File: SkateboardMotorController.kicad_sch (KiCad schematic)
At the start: 0 parts

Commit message: Added STM32
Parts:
- added C1: 0.1uF, symbol Device:C
- added FB1: FerriteBead, symbol Device:FerriteBead
- added U1: STM32F103C4Tx, Package_QFP:LQFP-48_7x7mm_P0.5mm, symbol MCU_ST_STM32F1:STM32F103C4Tx
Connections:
- new net: FB1.1, U1.9 (VDDA)
- new net +3.3V: C1.1, C1.2, FB1.2, U1.23 (VSS), U1.24 (VDD), U1.35 (VSS), U1.36 (VDD), U1.47 (VSS), U1.48 (VDD)

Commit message: finished most of STM32 and started on Gate drivers
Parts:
- added C2, C3, C4, C5: 0.1uF, symbol Device:C
- added R1, R2, R3: 10k, symbol Device:R
- added R4, R5: 10K, symbol Device:R
- added U2, U3, U5: IRS2104, Package_SO:SOIC-8_3.9x4.9mm_P1.27mm, symbol Driver_FET:IRS2104
- added Y1: MAX7375AXR805, Package_TO_SOT_SMD:SOT-323_SC-70, symbol Oscillator:MAX7375AXR805
- C1, FB1, U1: Manufacturer (none) -> Digikey
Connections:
- net +3.3V: now also C4.2, R1.1, R5.1, Y1.1 (V+); no longer C1.2, U1.23 (VSS), U1.35 (VSS), U1.47 (VSS)
- net Emergency Shutoff: now reaches U1.10 (PA0)
- net Emergency Shutoff: now also R5.2, U5.3 (~{SD})
- net at U1.20 (PB2): now also R3.1
- net PhaseA: now reaches U1.29 (PA8)
- net PhaseA: now also R4.1, U5.2 (IN)
- net at U1.44 (BOOT0): now also R2.1
- net at U1.5 (PD0): now also Y1.2 (CLOCK)
- net at U1.7 (NRST): now also C3.1, R1.2
- net GND: now reaches U1.8 (VSSA)
- net GND: now also C1.2, U1.23 (VSS), U1.35 (VSS), U1.47 (VSS), C2.2, C3.2, C4.1, C5.1, R2.2, R3.2, R4.2, U5.4 (COM), Y1.3 (GND)
- net at FB1.1, U1.9 (VDDA): now also C2.1
- new net +12V: C5.2, U5.1 (VCC)
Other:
- note added: "Gate Drivers"
- note added: "STM32 Microcontroller"
- moved on the sheet: FB1

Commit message: progress on gate drivers and found 60V-12V converter
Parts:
- added MP1: MP9486, Package_SO:SOIC-8-1EP_3.9x4.9mm_P1.27mm_EP2.41x3.3mm_ThermalVias, symbol MyLibrary:MP9486
- added R6, R7: 22, symbol Device:R
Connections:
- net at U5.5 (LO): now also R6.1
- net at U5.7 (HO): now also R7.1
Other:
- moved on the sheet: U2
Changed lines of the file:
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@@
+	)
+	(symbol
+		(lib_id "MyLibrary:MP9486")
+		(at 83.82 177.8 0)
+		(unit 1)
+		(exclude_from_sim no)
+		(in_bom yes)
+		(on_board yes)
+		(dnp no)
+		(property "Reference" "MP1"
+			(at 84.074 188.214 0)
+			(effects
+				(font
+					(size 1.27 1.27)
+				)
+			)
+		)
+		(property "Value" "MP9486"
+			(at 83.82 168.91 0)
+			(effects
+				(font
+					(size 1.27 1.27)
+				)
+			)
+		)
+		(property "Footprint" "Package_SO:SOIC-8-1EP_3.9x4.9mm_P1.27mm_EP2.41x3.3mm_ThermalVias"
+			(at 83.312 168.91 0)
+			(effects
+				(font
+					(size 1.27 1.27)
+				)
+				(hide yes)
+			)
+		)
+		(property "Datasheet" "https://www.monolithicpower.com/en/documentview/productdocument/index/version/2/document_type/Datasheet/lang/en/sku/MP9486/?srsltid=AU7gw4WBPXX73u71-zxU3O6eeoUXKs0Tn8aKEEhdp0QPcMegq4pCLmCL"
+			(at 83.82 177.8 0)
+			(effects
+				(font
+					(size 1.27 1.27)
+				)
+				(hide yes)
+			)
+		)
+		(property "Description" "60V -> 12V Buck converter, 1A max"
+			(at 83.82 177.8 0)
+			(effects
+				(font
+					(size 1.27 1.27)
+				)
+				(hide yes)
+			)
+		)
+		(property "Manufactuer PN" "MP9486GN-Z"
+			(at 83.82 177.8 0)
+			(effects
+				(font
+					(size 1.27 1.27)
+				)
+				(hide yes)
+			)
+		)
+		(property "Manufacturer" "JLCpcb"
+			(at 83.82 177.8 0)
+			(effects
+				(font
+					(size 1.27 1.27)
+				)
+				(hide yes)
+			)
+		)
+		(pin "4"
+		)
+		(pin "1"
+		)
+		(pin "6"
+		)
+		(pin "8"
+		)
+		(pin "7"
+		)
+		(pin "3"
+		)
+		(pin "2"
+		)
+		(pin "5"
+		)
+		(instances
+			(project ""
+				(path "/51090867-fcd4-4552-acda-4929fd1c7810"
+					(reference "MP1")
+					(unit 1)
+				)
+			)
+		)
 	)
 	(symbol
@@
 	(symbol
 		(lib_id "Driver_FET:IRS2104")
-		(at 271.78 58.42 0)
+		(at 283.21 57.15 0)
 		(unit 1)
 		(exclude_from_sim no)
@@
 		(fields_autoplaced yes)
 		(property "Reference" "U2"
-			(at 273.9233 43.18 0)
+			(at 285.3533 41.91 0)
 			(effects
 				(font
@@
 		)
 		(property "Value" "IRS2104"
-			(at 273.9233 45.72 0)
+			(at 285.3533 44.45 0)
 			(effects
 				(font
@@
 		)
 		(property "Footprint" "Package_SO:SOIC-8_3.9x4.9mm_P1.27mm"
-			(at 271.78 58.42 0)
+			(at 283.21 57.15 0)
 			(effects
 				(font
@@
 		)
 		(property "Datasheet" "https://www.infineon.com/dgdl/irs2104.pdf?fileId=5546d462533600a40153567633f727a1"
-			(at 271.78 58.42 0)
+			(at 283.21 57.15 0)
 			(effects
 				(font
@@
 		)
 		(property "Description" "Half-Bridge Driver, 600V, 290/600mA, PDIP-8/SOIC-8"
-			(at 271.78 58.42 0)
+			(at 283.21 57.15 0)
 			(effects
 				(font
@@
 	(symbol
 		(lib_id "Device:R")
+		(at 251.46 53.34 90)
+		(unit 1)
+		(exclude_from_sim no)
+		(in_bom yes)
+		(on_board yes)
+		(dnp no)
+		(fields_autoplaced yes)
+		(property "Reference" "R7"
+			(at 251.46 46.99 90)
+			(effects
+				(font
+					(size 1.27 1.27)
+				)
+			)
+		)
+		(property "Value" "22"
+			(at 251.46 49.53 90)
+			(effects
+				(font
+					(size 1.27 1.27)
+				)
+			)
+		)
+		(property "Footprint" ""
+			(at 251.46 55.118 90)
+			(effects
+				(font
+					(size 1.27 1.27)
+				)
+				(hide yes)
+			)
+		)
+		(property "Datasheet" "~"
+			(at 251.46 53.34 0)
+			(effects
+				(font
+					(size 1.27 1.27)
+				)
+				(hide yes)
+			)
+		)
+		(property "Description" "Resistor"
+			(at 251.46 53.34 0)
+			(effects
+				(font
+					(size 1.27 1.27)
+				)
+				(hide yes)
+			)
+		)
+		(pin "2"
+		)
+		(pin "1"
+		)
+		(instances
+			(project "SkateboardMotorController"
+				(path "/51090867-fcd4-4552-acda-4929fd1c7810"
+					(reference "R7")
+					(unit 1)
+				)
+			)
+		)
+	)
+	(symbol
+		(lib_id "Device:R")
 		(at 120.65 90.17 0)
 		(unit 1)
@@
 					(unit 1)
 				)
+			)
+		)
+	)
+	(symbol
+		(lib_id "Device:R")
+		(at 251.46 66.04 90)
+		(unit 1)
+		(exclude_from_sim no)
+		(in_bom yes)
+		(on_board yes)
+		(dnp no)
+		(fields_autoplaced yes)
+		(property "Reference" "R6"
+			(at 251.46 59.69 90)
+			(effects
+				(font
+					(size 1.27 1.27)
+				)
+			)
+		)
+		(property "Value" "22"
+			(at 251.46 62.23 90)
+			(effects
+				(font
+					(size 1.27 1.27)
+				)
+			)
+		)
+		(property "Footprint" ""
+			(at 251.46 67.818 90)
+			(effects
+				(font
+					(size 1.27 1.27)
+				)
+				(hide yes)
+			)
+		)
+		(property "Datasheet" "~"
+			(at 251.46 66.04 0)
+			(effects
+				(font
+					(size 1.27 1.27)
+				)
+				(hide yes)
+			)
+		)
+		(property "Description" "Resistor"
+			(at 251.46 66.04 0)
+			(effects
+				(font
+					(size 1.27 1.27)
+				)
+				(hide yes)
+			)
+		)
+		(pin "2"
+		)
+		(pin "1"
+		)
+		(instances
+			(project ""
+				(path "/51090867-fcd4-4552-acda-4929fd1c7810"
+					(reference "R6")
+					(unit 1)
+				)

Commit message: finished 12V rail
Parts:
- added B1100LB-13-F: 1A/100V, Diode_SMD:D_SMB, symbol Device:D_Schottky
- added C10: 10uF, Capacitor_SMD:C_0805_2012Metric, symbol Device:C
- added C11: 100uF/25V, Capacitor_Tantalum_SMD:CP_EIA-7343-43_Kemet-X, symbol Device:C_Polarized
- added C6, C8: 2.2uF/100V, Capacitor_SMD:C_1206_3216Metric, symbol Device:C
- added C7, C9: 0.1uF, Capacitor_SMD:C_0603_1608Metric, symbol Device:C
- added L1: 47uH, Inductor_SMD:L_Bourns_SRN6045TA, symbol Device:L
- added R10: 4.7k, Resistor_SMD:R_0603_1608Metric, symbol Device:R
- added R8: 590k, Resistor_SMD:R_0603_1608Metric, symbol Device:R
- added R9: 10k, Resistor_SMD:R_0603_1608Metric, symbol Device:R
- C1, C2, C3, C4, C5: footprint (none) -> Capacitor_SMD:C_0603_1608Metric
- MP1: value MP9486 -> ~; Manufactuer PN MP9486GN-Z -> (none); Manufacturer JLCpcb -> (none)
- R1, R2, R3, R4, R5, R6, R7: footprint (none) -> Resistor_SMD:R_0603_1608Metric
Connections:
- net +12V: now also C10.1, C11.1, C9.2, L1.2, R8.2
- net GND: now also MP1.6 (DIM), MP1.7 (EN), MP1.8 (GND), B1100LB-13-F.2 (A), C10.2, C11.2, C6.2, C8.2, R9.1
- net at MP1.1 (FB): now also R10.1, R8.1, R9.2
- net +40V: now reaches MP1.3 (VIN)
- net +40V: now also C6.1, C8.1
- net at MP1.4 (BST): now also C7.1
- net at MP1.5 (SW): now also B1100LB-13-F.1 (K), C7.2, L1.1
- new net: C9.1, R10.2

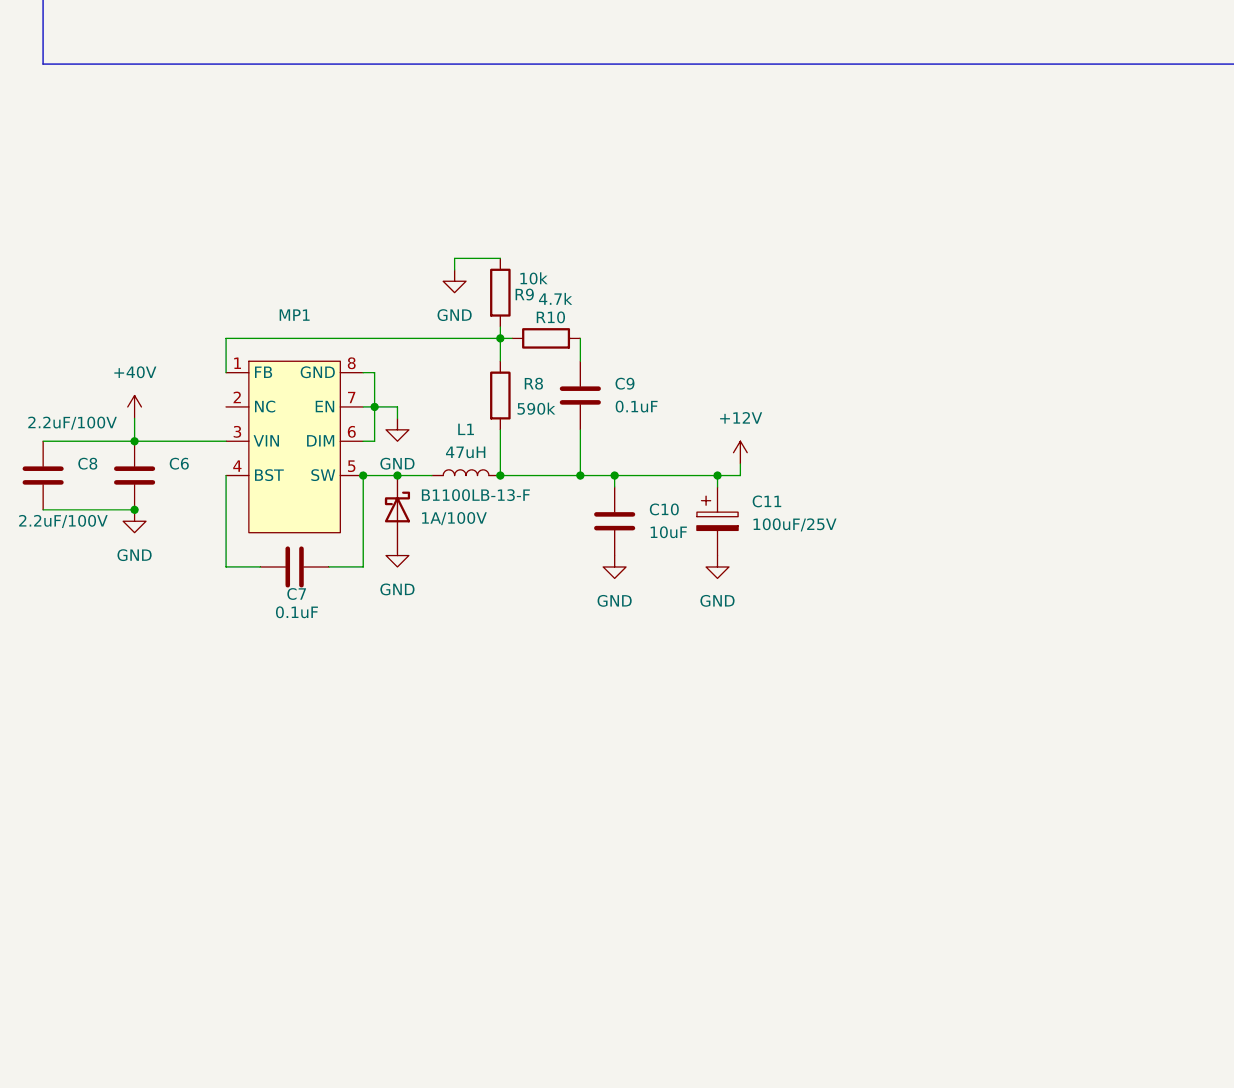
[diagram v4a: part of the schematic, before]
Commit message: added 3.3V rail
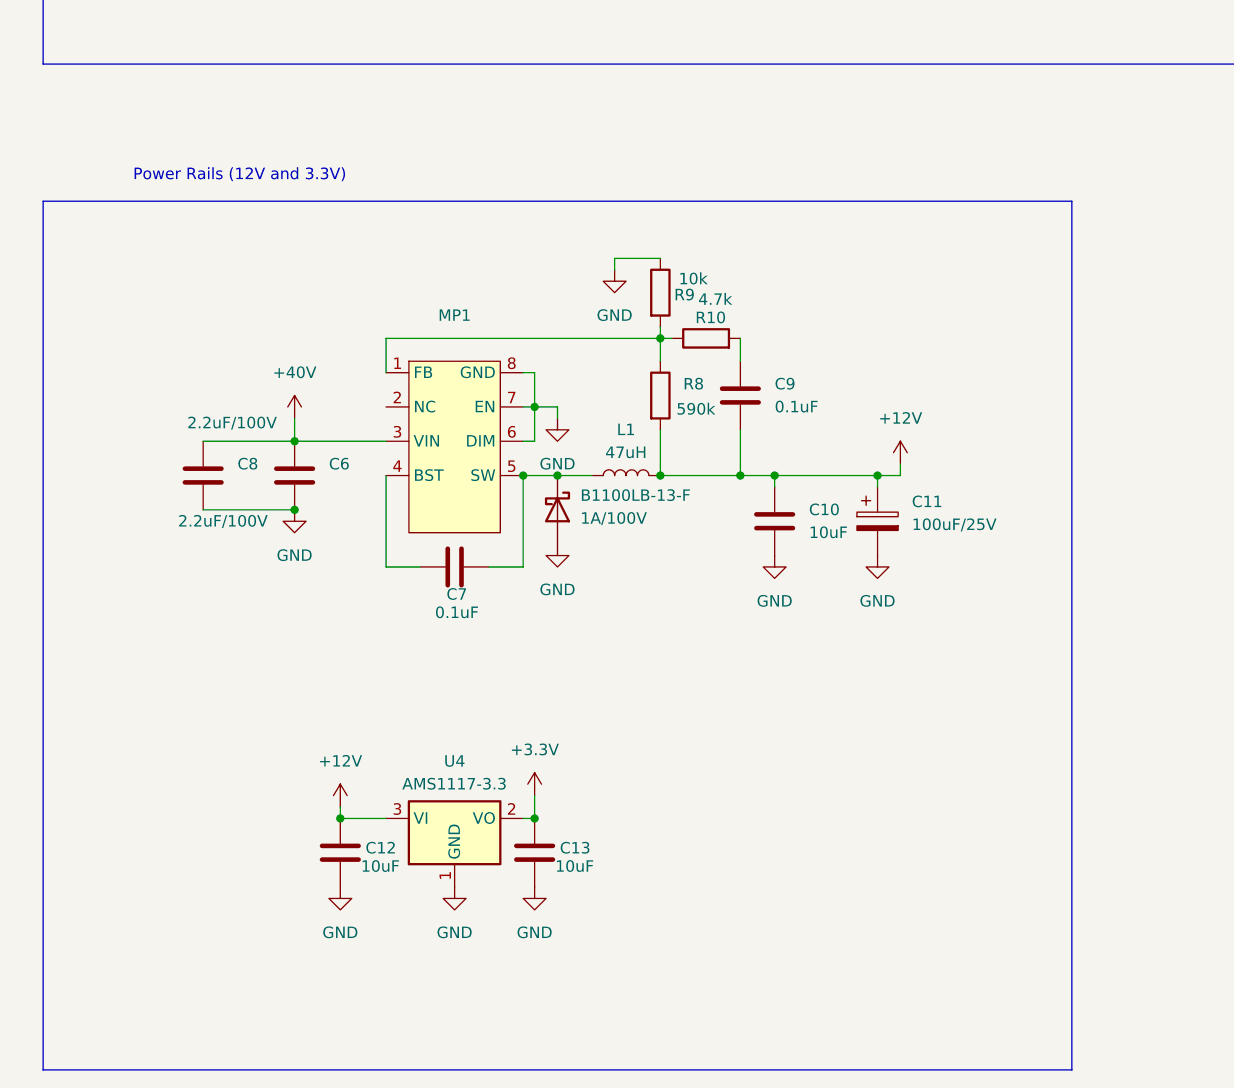
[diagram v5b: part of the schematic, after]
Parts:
- added C12, C13: 10uF, Capacitor_SMD:C_0805_2012Metric, symbol Device:C
- added U4: AMS1117-3.3, Package_TO_SOT_SMD:SOT-223-3_TabPin2, symbol Regulator_Linear:AMS1117-3.3
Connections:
- net +12V: now also C12.1, U4.3 (VI)
- net +3.3V: now also C13.1, U4.2 (VO)
- net GND: now also C12.2, C13.2, U4.1 (GND)
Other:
- note added: "Power Rails (12V and 3.3V)"
- moved on the sheet: B1100LB-13-F, C10, C11, C6, C7, C8, C9, L1, MP1, R10, R8, R9
